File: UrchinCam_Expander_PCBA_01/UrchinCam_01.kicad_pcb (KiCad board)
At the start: 4 copper layers, 31.5 x 65 mm, 90 parts, among them J1 95157-440LF, J2 SM04B-GHS, J3 SM04B-GHS, J4 SM02B-GHS, J5 SM04B-GHS, U1 MP6550, U2 ADS1115IDGS, U3 BNO085, U4 TSR3-2450N, U5 RTL8152B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

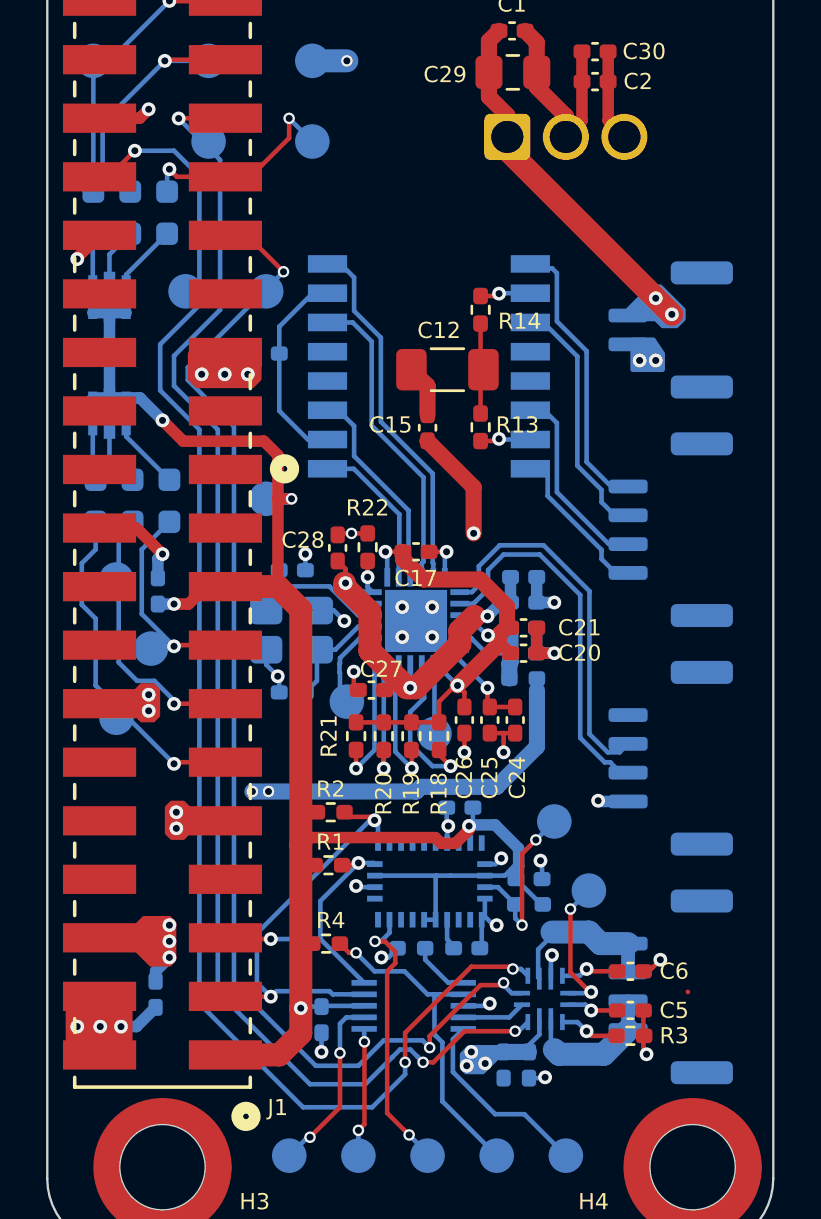
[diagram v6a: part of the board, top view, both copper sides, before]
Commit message: Fixed all DRC errors.
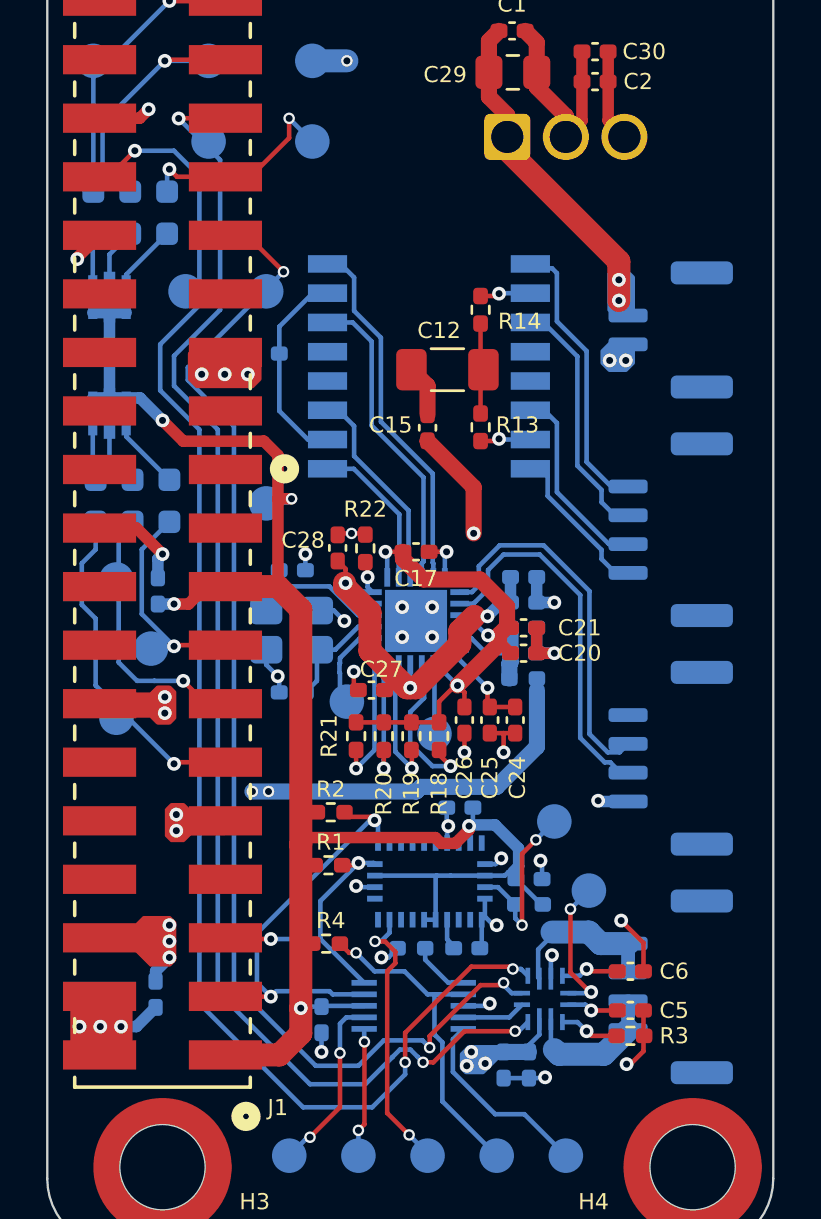
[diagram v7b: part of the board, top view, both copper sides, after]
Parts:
- moved TP3 0.20 mm to (144.5, 103.2)
- moved R22 0.11 mm to (148.8, 105.2)
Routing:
- net GND: track 60.2 -> 63.8 mm
- net Net-(J4-Pin_1): track 16.1 -> 14.6 mm
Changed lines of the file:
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@@
 	(footprint "Resistor_SMD:R_0402_1005Metric_Pad0.72x0.64mm_HandSolder"
 		(layer "F.Cu")
-		(at 148.9 105.1 -90)
+		(at 148.8 105.1525 -90)
 		(descr "Resistor SMD 0402 (1005 Metric), square (rectangular) end terminal, IPC-7351 nominal with elongated pad for handsoldering. (Body size source: IPC-SM-782 page 72, https://www.pcb-3d.com/wordpress/wp-content/uploads/ipc-sm-782a_amendment_1_and_2.pdf), generated with kicad-footprint-generator")
 		(tags "resistor handsolder")
@@
 		(fp_text user "*"
 			(at -1.989099 1 90)
-			(unlocked yes)
-			(layer "B.SilkS")
-			(effects
-				(font
-					(size 1 1)
-					(thickness 0.15)
-				)
-				(justify mirror)
-			)
-		)
-		(fp_text user "*"
-			(at -1.989099 1 90)
 			(layer "B.SilkS")
 			(effects
@@
 	(footprint "TestPoint:TestPoint_Pad_D1.5mm"
 		(layer "B.Cu")
-		(at 144.5 103 180)
+		(at 144.5 103.2 180)
 		(descr "SMD pad as test Point, diameter 1.5mm")
 		(tags "test point SMD pad")
@@
 		(fp_text user "*"
 			(at 1.4478 0.8128 90)
-			(unlocked yes)
-			(layer "B.SilkS")
-			(effects
-				(font
-					(size 1 1)
-					(thickness 0.15)
-				)
-				(justify mirror)
-			)
-		)
-		(fp_text user "*"
-			(at 1.4478 0.8128 90)
 			(layer "B.SilkS")
 			(effects
@@
 		)
 		(fp_text user "*"
-			(at -2.928899 1.5 90)
-			(layer "B.SilkS")
-			(effects
-				(font
-					(size 1 1)
-					(thickness 0.15)
-				)
-				(justify mirror)
-			)
-		)
-		(fp_text user "*"
 			(at -1.4859 1.5 90)
 			(layer "B.Fab")
@@
 	(gr_poly
 		(pts
-			(xy 142.7 116.5) (xy 141.2 116.5) (xy 140.9 116.2) (xy 140.4 116.2) (xy 140.2 116.4) (xy 140.2 117.5)
-			(xy 140.4 117.7) (xy 140.9 117.7) (xy 141.2 117.4) (xy 142.7 117.4)
+			(xy 142.7 116.6) (xy 141.2 116.6) (xy 140.9 116.3) (xy 140.4 116.3) (xy 140.2 116.5) (xy 140.2 117.6)
+			(xy 140.4 117.8) (xy 140.9 117.8) (xy 141.2 117.5) (xy 142.7 117.5)
 		)
 		(stroke
@@
 	(gr_poly
 		(pts
-			(xy 135.9 124.7) (xy 135.9 127.1) (xy 138.6 127.1) (xy 138.6 124.7)
+			(xy 136.1 124.614409) (xy 136.1 127.014409) (xy 138.6 127.014409) (xy 138.6 124.614409)
 		)
 		(stroke
@@
 	(gr_poly
 		(pts
-			(xy 137.3 112.3) (xy 138.8 112.3) (xy 139.1 112.6) (xy 139.6 112.6) (xy 139.8 112.4) (xy 139.8 111.3)
-			(xy 139.6 111.1) (xy 139.1 111.1) (xy 138.8 111.4) (xy 137.3 111.4)
+			(xy 138 112.4) (xy 139.5 112.4) (xy 139.8 112.7) (xy 140.3 112.7) (xy 140.5 112.5) (xy 140.5 111.4)
+			(xy 140.3 111.2) (xy 139.8 111.2) (xy 139.5 111.5) (xy 138 111.5)
 		)
 		(stroke
@@
 	(gr_poly
 		(pts
-			(xy 160.2 95.2) (xy 161.4 95.2) (xy 161.7 95.5) (xy 162.3 95.5) (xy 162.6 95.2) (xy 162.6 94.8) (xy 161.6 93.8)
-			(xy 161.2 93.8) (xy 160.2 94.8)
+			(xy 159.6 95) (xy 160.4 95) (xy 160.4 93.4) (xy 160 93) (xy 159.6 93) (xy 159.4 93.2) (xy 159.4 94.8)
 		)
 		(stroke
@@
 	(gr_poly
 		(pts
-			(xy 160.4 96.1) (xy 161.3 96.1) (xy 161.7 96.7) (xy 161.7 97.4) (xy 160.4 97.4)
+			(xy 159.1 96.6) (xy 159.5 96.2) (xy 160.2 96.2) (xy 160.4 96.450001) (xy 160.4 97.1) (xy 160.1 97.4)
+			(xy 159.4 97.4) (xy 159.1 97.1)
 		)
 		(stroke
@@
 	(gr_poly
 		(pts
-			(xy 140.1 125.2) (xy 136.4 125.2) (xy 136 125.6) (xy 136 126.2) (xy 137.2 127.4) (xy 140.1 127.4)
+			(xy 140.1 125.2) (xy 136.4 125.2) (xy 136.1 125.5) (xy 136.1 126.3) (xy 137.2 127.4) (xy 140.1 127.4)
 		)
 		(stroke
@@
 	)
 	(gr_text "3V3"
-		(at 143.3 101.6 90)
+		(at 143.3 101.8 90)
 		(layer "B.SilkS")
 		(effects
@@
 	)
 	(segment
+		(start 160.8675 122.2675)
+		(end 159.9 121.3)
+		(width 0.2)
+		(layer "F.Cu")
+		(net 1)
+	)
+	(segment
 		(start 137.27 104.27)
 		(end 138.870999 104.27)
@@
 	)
 	(segment
-		(start 161.1 123.5)
-		(end 161.6 123)
+		(start 160.306436 127.528564)
+		(end 160.8675 126.9675)
 		(width 0.2)
 		(layer "F.Cu")
@@
 	)
 	(segment
-		(start 160.8675 126.9675)
-		(end 161 127.1)
-		(width 0.2)
-		(layer "F.Cu")
-		(net 1)
-	)
-	(segment
 		(start 136.3 92.6)
 		(end 136.3 92.54)
@@
 	)
 	(segment
-		(start 160.8675 125.2)
-		(end 160.8675 126.9675)
-		(width 0.2)
-		(layer "F.Cu")
-		(net 1)
-	)
-	(segment
 		(start 151.5 100.485)
 		(end 151.5 100.5)
@@
 	)
 	(segment
-		(start 160.8675 123.5)
-		(end 161.1 123.5)
-		(width 0.2)
+		(start 157.5 86.4)
+		(end 157.5 87.3)
+		(width 0.7)
 		(layer "F.Cu")
 		(net 1)
 	)
 	(segment
-		(start 157.5 86.4)
-		(end 157.5 87.3)
-		(width 0.7)
+		(start 160.13565 127.528564)
+		(end 160.306436 127.528564)
+		(width 0.2)
 		(layer "F.Cu")
 		(net 1)
@@
 	)
 	(segment
+		(start 160.8675 126.9675)
+		(end 160.8675 125.2)
+		(width 0.2)
+		(layer "F.Cu")
+		(net 1)
+	)
+	(segment
 		(start 156.2375 84.5)
 		(end 156.2375 83.2025)
@@
 	)
 	(segment
+		(start 160.8675 123.5)
+		(end 160.8675 122.2675)
+		(width 0.2)
+		(layer "F.Cu")
+		(net 1)
+	)
+	(segment
 		(start 148.5 111.3)
 		(end 148.3 111.1)
@@
 	)
 	(via
-		(at 160.7 97)
+		(at 159.4 97)
 		(size 0.6)
 		(drill 0.3)
@@
 	)
 	(via
-		(at 161.6 123)
-		(size 0.6)
-		(drill 0.3)
-		(layers "F.Cu" "B.Cu")
-		(net 1)
-	)
-	(via
 		(at 154.7 118.6)
 		(size 0.6)
@@
 	)
 	(via
-		(at 161.4 97)
+		(at 160.1 97)
 		(size 0.6)
 		(drill 0.3)
@@
 	)
 	(via
+		(at 159.9 121.3)
+		(size 0.6)
+		(drill 0.3)
+		(layers "F.Cu" "B.Cu")
+		(net 1)
+	)
+	(via
 		(at 144.9 79.2)
 		(size 0.6)
@@
 	)
 	(via
-		(at 140.6 117.3)
+		(at 140.6 117.4)
 		(size 0.6)
 		(drill 0.3)
@@
 	)
 	(via
-		(at 139.4 112.2)
+		(at 140.1 112.3)
 		(size 0.6)
 		(drill 0.3)
@@
 	)
 	(via
-		(at 140.6 116.6)
+		(at 140.6 116.7)
 		(size 0.6)
 		(drill 0.3)
@@
 	)
 	(via
-		(at 161 127.1)
+		(at 160.13565 127.528564)
 		(size 0.6)
 		(drill 0.3)
@@
 	)
 	(via
-		(at 139.4 111.5)
+		(at 140.1 111.6)
 		(size 0.6)
 		(drill 0.3)
@@
 	)
 	(segment
+		(start 154.8 128.135)
+		(end 155.9 128.135)
+		(width 0.2)
+		(layer "B.Cu")
+		(net 1)
+	)
+	(segment
 		(start 150.2025 122.5)
 		(end 149.8025 122.9)
@@
 	(segment
 		(start 154.96 87.3)
-		(end 154.96 86.36)
-		(width 0.7)
+		(end 154.96 87.86)
+		(width 1)
 		(layer "F.Cu")
 		(net 2)
 	)
 	(segment
-		(start 154.96 86.36)
-		(end 154.1625 85.5625)
-		(width 0.7)
+		(start 159.8 92.7)
+		(end 159.8 94.4)
+		(width 1)
 		(layer "F.Cu")
 		(net 2)
@@
 	(segment
 		(start 154.96 87.3)
-		(end 154.96 87.86)
-		(width 1)
+		(end 154.96 86.36)
+		(width 0.7)
 		(layer "F.Cu")
 		(net 2)
 	)
 	(segment
-		(start 154.96 87.86)
-		(end 162.1 95)
-		(width 1)
+		(start 154.96 86.36)
+		(end 154.1625 85.5625)
+		(width 0.7)
 		(layer "F.Cu")
 		(net 2)
@@
 		(net 2)
 	)
+	(segment
+		(start 154.96 87.86)
+		(end 159.8 92.7)
+		(width 1)
+		(layer "F.Cu")
+		(net 2)
+	)
 	(via
-		(at 162.1 95)
+		(at 159.8 93.5)
 		(size 0.6)
 		(drill 0.3)
@@
 	)
 	(via
-		(at 161.4 94.3)
+		(at 159.8 94.4)
 		(size 0.6)
 		(drill 0.3)
@@
 	)
 	(via
-		(at 136.3 125.9)
+		(at 136.4 125.9)
 		(size 0.6)
 		(drill 0.3)
@@
 	)
 	(segment
-		(start 140.51 111.89)
-		(end 140.5 111.9)
+		(start 141.89 111.89)
+		(end 142.731 111.89)
 		(width 0.2)
 		(layer "F.Cu")
@@
 	)
 	(segment
-		(start 142.731 111.89)
-		(end 140.51 111.89)
+		(start 140.9 110.9)
+		(end 141.89 111.89)
 		(width 0.2)
 		(layer "F.Cu")
@@
 	)
 	(via
-		(at 140.5 111.9)
+		(at 140.9 110.9)
 		(size 0.6)
 		(drill 0.3)
@@
 	)
 	(segment
-		(start 138.1 110.1)
-		(end 138.1 104.6)
+		(start 138.899 110.899)
+		(end 138.1 110.1)
 		(width 0.2)
 		(layer "B.Cu")
@@
 	)
 	(segment
-		(start 138.899 110.899)
-		(end 138.1 110.1)
+		(start 138.1 104.6)
+		(end 138.7 104)
 		(width 0.2)
 		(layer "B.Cu")
@@
 	)
 	(segment
-		(start 138.1 104.6)
-		(end 138.7 104)
+		(start 139.648943 110.899)
+		(end 138.899 110.899)
 		(width 0.2)
 		(layer "B.Cu")
@@
 	)
 	(segment
-		(start 140.5 111.750057)
-		(end 139.648943 110.899)
+		(start 140.9 110.9)
+		(end 139.649943 110.9)
 		(width 0.2)
 		(layer "B.Cu")
@@
 	)
 	(segment
-		(start 139.648943 110.899)
-		(end 138.899 110.899)
+		(start 139.649943 110.9)
+		(end 139.648943 110.899)
 		(width 0.2)
 		(layer "B.Cu")
@@
 	)
 	(segment
-		(start 140.5 111.9)
-		(end 140.5 111.750057)
+		(start 138.1 110.1)
+		(end 138.1 104.6)
 		(width 0.2)
 		(layer "B.Cu")
@@
 	)
 	(segment
-		(start 162.8 124.4)
-		(end 162.789 124.389)
-		(width 0.2)
-		(layer "F.Cu")
-		(net 71)
-	)
-	(segment
 		(start 157.7 120.8)
 		(end 157.7 123.549943)
@@
 		(polygon
 			(pts
-				(xy 160 100) (xy 159 99) (xy 159 94) (xy 155.5 90.5) (xy 148 90.5) (xy 146.5 92) (xy 146.5 102.2)
-				(xy 148.3 104) (xy 156 104) (xy 160.5 108.5) (xy 168 108.5) (xy 168 137) (xy 133.5 137) (xy 133.5 69.5)
-				(xy 168 69.5) (xy 168 100)
+				(xy 160 100) (xy 159 99) (xy 159 95.6) (xy 158.5 95.1) (xy 158.5 93.5) (xy 155.5 90.5) (xy 148 90.5)
+				(xy 146.5 92) (xy 146.5 102.2) (xy 148.3 104) (xy 156 104) (xy 160.5 108.5) (xy 168 108.5) (xy 168 137)
+				(xy 133.5 137) (xy 133.5 69.5) (xy 168 69.5) (xy 168 100)
 			)
 		)
@@
 		(polygon
 			(pts
-				(xy 160 100) (xy 159 99) (xy 159 94) (xy 155.5 90.5) (xy 148 90.5) (xy 146.5 92) (xy 146.5 102.2)
-				(xy 148.3 104) (xy 156 104) (xy 160.5 108.5) (xy 168 108.5) (xy 168 137) (xy 133.5 137) (xy 133.5 69.5)
-				(xy 168 69.5) (xy 168 100)
+				(xy 160 100) (xy 159 99) (xy 159 95.6) (xy 158.5 95.1) (xy 158.5 93.5) (xy 155.5 90.5) (xy 148 90.5)
+				(xy 146.5 92) (xy 146.5 102.2) (xy 148.3 104) (xy 156 104) (xy 160.5 108.5) (xy 168 108.5) (xy 168 137)
+				(xy 133.5 137) (xy 133.5 69.5) (xy 168 69.5) (xy 168 100)
 			)
 		)
